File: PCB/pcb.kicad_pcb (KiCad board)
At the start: 2 copper layers, 3.9 x 3.7 mm, 320 parts, among them J1 USB_C_Receptacle_USB2.0, SW1 SW_Push, U1 AT90USB1286-AU, Y1 Crystal_GND24_Small

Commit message: Diode placement, Alternative Bottom Rows
-New Footprints
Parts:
- added MX101: MX-NoLED, kailh-switches-hotswap:Kailh-Hotswap-6.25U, F.Cu at (220.7, 361.9)
- added MX102: MX-NoLED, kailh-switches-hotswap:Kailh-Hotswap-7U, F.Cu at (227.8, 361.9)
- added MX103: MX-NoLED, kailh-switches-hotswap:Kailh-Hotswap-1U, F.Cu at (289.7, 361.9)
- added MX104: MX-NoLED, kailh-switches-hotswap:Kailh-Hotswap-1.25U, F.Cu at (306.4, 361.9)
- MX11: footprint kailh-switches-hotswap:Kailh-Hotswap-1.25U -> kailh-switches-hotswap:Kailh-Hotswap-1U
- MX6: footprint kailh-switches-hotswap:Kailh-Hotswap-1.25U -> kailh-switches-hotswap:Kailh-Hotswap-1.5U
- MX80: footprint kailh-switches-hotswap:Kailh-Hotswap-1U -> kailh-switches-hotswap:Kailh-Hotswap-2U
- MX88: footprint kailh-switches-hotswap:Kailh-Hotswap-2U -> kailh-switches-hotswap:Kailh-Hotswap-1U
- moved D95 570.5 mm to (455.6, 308.8), turned to 90 degrees
- moved D90 563.0 mm to (436.6, 308.8), turned to 90 degrees
- moved D85 555.2 mm to (417.5, 308.8), turned to 90 degrees
- moved D91 545.8 mm to (436.6, 327.8), turned to 90 degrees
- moved D86 544.5 mm to (417.5, 327.8), turned to 90 degrees
- moved D87 525.3 mm to (417.5, 346.9), turned to 90 degrees
- moved D88 515.9 mm to (427.0, 365.9), turned to 90 degrees
- moved D79 438.9 mm to (388.9, 265.9), turned to 90 degrees
- moved D1 431.6 mm to (93.7, 265.9), turned to 90 degrees
- moved D24 431.5 mm to (169.9, 289.7), turned to 90 degrees
- moved D39 431.2 mm to (236.5, 265.9), turned to 90 degrees
- moved D33 427.1 mm to (217.5, 265.9), turned to 90 degrees
- moved D50 414.9 mm to (265.1, 289.7), turned to 90 degrees
- moved D45 412.5 mm to (246.1, 289.7), turned to 90 degrees
- moved D7 411.7 mm to (112.7, 289.7), turned to 90 degrees
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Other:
- board size 3.9 x 3.7 mm -> 827.1 x 748.5 mm

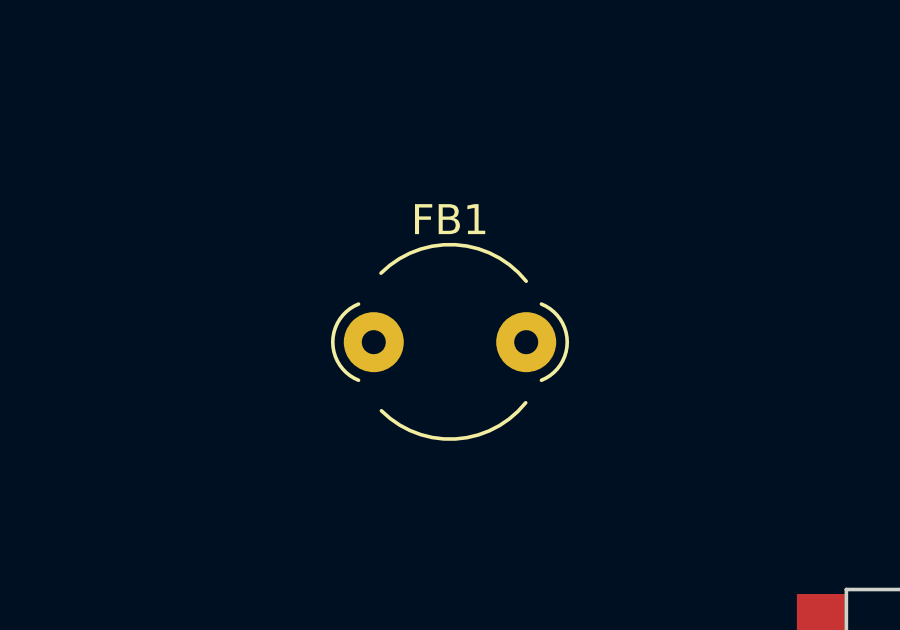
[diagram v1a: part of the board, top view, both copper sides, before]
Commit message: Changed Footprint for Ferrite
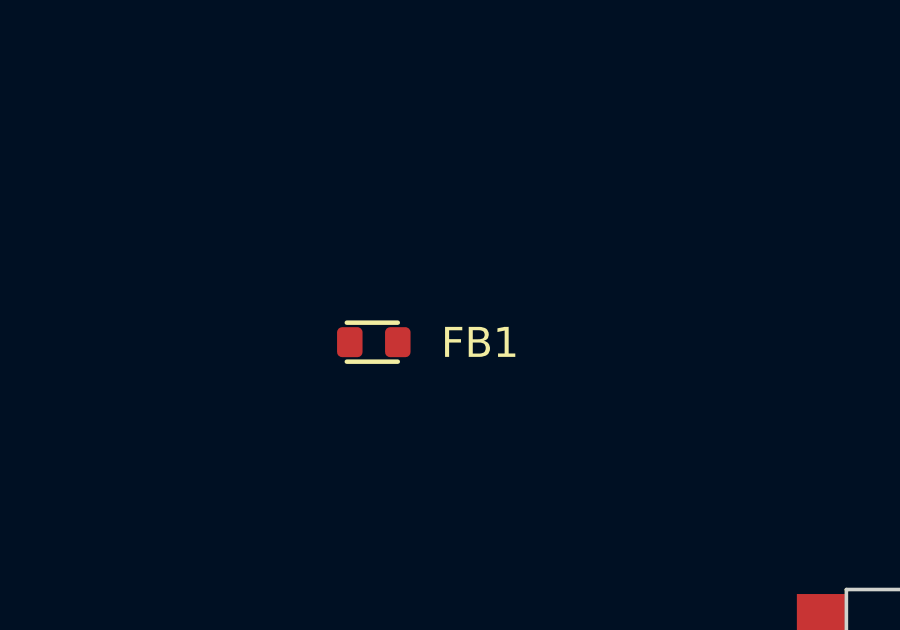
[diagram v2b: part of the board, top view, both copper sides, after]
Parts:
- FB1: footprint Ferrite_THT:LairdTech_28C0236-0JW-10 -> josh-passives-smt:Ferrite_Bead_0603
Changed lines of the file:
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@@
     )
   )
-  (footprint "Ferrite_THT:LairdTech_28C0236-0JW-10" (layer "F.Cu")
+  (footprint "josh-passives-smt:Ferrite_Bead_0603" (layer "F.Cu")
     (at 94.495332 474.8275)
-    (descr "Ferrite, vertical, LairdTech 28C0236-0JW-10, https://assets.lairdtech.com/home/brandworld/files/28C0236-0JW-10.pdf, JW Miller core https://www.bourns.com/products/magnetic-products/j.w.-miller-through-hole-ferrite-beads-emi-filters")
-    (tags "Ferrite vertical LairdTech 28C0236-0JW-10")
+    (descr "ferrite bead 0603")
+    (tags "Ferrite Bead")
     (property "Sheetfile" "pcb.kicad_sch")
     (property "Sheetname" "")
-    (attr through_hole)
-    (fp_text reference "FB1" (at 2.54 -4.064) (layer "F.SilkS")
+    (attr smd)
+    (fp_text reference "FB1" (at 3.542 0.028) (layer "F.SilkS")
       (effects (font (size 1 1) (thickness 0.15)))
     )
-    (fp_text value "600R" (at 2.54 4.953) (layer "F.Fab")
-      (effects (font (size 1 1) (thickness 0.15)))
+    (fp_text value "600R" (at 0 1.9) (layer "F.Fab") hide
+      (effects (font (size 1.27 1.27) (thickness 0.254)))
     )
-    (fp_text user "${REFERENCE}" (at 2.54 0) (layer "F.Fab")
-      (effects (font (size 1 1) (thickness 0.15)))
-    )
-    (fp_arc (start 5.588 -1.27) (mid 6.447832 0) (end 5.588 1.27) (layer "F.SilkS") (width 0.12))
-    (fp_arc (start 0.239932 -2.300068) (mid 2.71988 -3.24781) (end 5.08 -2.032) (layer "F.SilkS") (width 0.12))
-    (fp_arc (start 5.064465 2.019572) (mid 2.71878 3.227946) (end 0.254 2.286) (layer "F.SilkS") (width 0.12))
-    (fp_arc (start -0.508 1.27) (mid -1.367832 0) (end -0.508 -1.27) (layer "F.SilkS") (width 0.12))
-    (fp_circle (center 2.54 0) (end 6.48 0) (layer "F.CrtYd") (width 0.05) (fill none))
-    (fp_line (start 0 -1.145) (end 5.08 -1.145) (layer "F.Fab") (width 0.1))
-    (fp_line (start 0 1.145) (end 5.08 1.145) (layer "F.Fab") (width 0.1))
-    (fp_arc (start 0 1.145) (mid -1.145 0) (end 0 -1.145) (layer "F.Fab") (width 0.1))
-    (fp_arc (start 5.08 -1.145) (mid 6.225 0) (end 5.08 1.145) (layer "F.Fab") (width 0.1))
-    (fp_circle (center 2.54 0) (end 5.54 0) (layer "F.Fab") (width 0.1) (fill none))
-    (pad "1" thru_hole circle (at 0 0) (size 2 2) (drill 0.8) (layers *.Cu *.Mask)
+    (fp_line (start -0.9 -0.65) (end 0.8 -0.65) (layer "F.SilkS") (width 0.15))
+    (fp_line (start -0.9 0.65) (end 0.8 0.65) (layer "F.SilkS") (width 0.15))
+    (fp_line (start 0.8 -0.4) (end 0.8 0.4) (layer "Dwgs.User") (width 0.1))
+    (fp_line (start -0.8 0.4) (end -0.8 -0.4) (layer "Dwgs.User") (width 0.1))
+    (fp_line (start -1.475 0.75) (end -1.475 -0.75) (layer "F.CrtYd") (width 0.05))
+    (fp_line (start 1.475 0.75) (end -1.475 0.75) (layer "F.CrtYd") (width 0.05))
+    (fp_line (start -1.475 -0.75) (end 1.475 -0.75) (layer "F.CrtYd") (width 0.05))
+    (fp_line (start 1.475 -0.75) (end 1.475 0.75) (layer "F.CrtYd") (width 0.05))
+    (pad "1" smd roundrect (at -0.8 0) (size 0.85 1) (layers "F.Cu" "F.Paste" "F.Mask") (roundrect_rratio 0.2)
       (net 3 "+5V") (pintype "passive"))
-    (pad "2" thru_hole circle (at 5.08 0) (size 2 2) (drill 0.8) (layers *.Cu *.Mask)
+    (pad "2" smd roundrect (at 0.8 0) (size 0.85 1) (layers "F.Cu" "F.Paste" "F.Mask") (roundrect_rratio 0.2)
       (net 214 "Net-(F1-Pad1)") (pintype "passive"))
-    (model "${KICAD6_3DMODEL_DIR}/Ferrite_THT.3dshapes/LairdTech_28C0236-0JW-10.wrl"
+    (model "${KIPRJMOD}/../../josh-kicad-lib//packages3d/josh-passives-smt/BLM18PG121SZ1D.stp"
       (offset (xyz 0 0 0))
       (scale (xyz 1 1 1))

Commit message: Placed all LEDs
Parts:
- MX80: footprint kailh-switches-hotswap:Kailh-Hotswap-2U -> kailh-switches-hotswap:Kailh-Hotswap-1U
- MX88: footprint kailh-switches-hotswap:Kailh-Hotswap-1U -> kailh-switches-hotswap:Kailh-Hotswap-2U
- moved D196 624.6 mm to (462.8, 236.5)
- moved D199 590.3 mm to (481.8, 227.0)
- moved D154 563.8 mm to (310.4, 174.6)
- moved D189 554.7 mm to (443.7, 198.4)
- moved D139 543.5 mm to (243.7, 174.6)
- moved D168 540.8 mm to (338.9, 217.5)
- moved D192 528.7 mm to (443.7, 255.6)
- moved D185 513.3 mm to (424.7, 217.5)
- moved D169 510.0 mm to (343.7, 236.5)
- moved D194 508.0 mm to (462.8, 198.4)
- moved D118 494.0 mm to (158.0, 174.6)
- moved D155 481.2 mm to (291.3, 198.4)
- moved D184 470.3 mm to (424.7, 198.4)
- moved D182 465.8 mm to (396.1, 236.5)
- moved D144 463.3 mm to (262.7, 174.6)
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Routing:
- net +5V: track 26.6 -> 0.63 mm
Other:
- board size 827.1 x 748.5 mm -> 403.2 x 127 mm

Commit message: PCB Size, LED Footprints
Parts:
- D1, D10, D100, D11, D12, D13, D14, D15, D16, D17, D18, D19, D2, D20, D21, D22, D23, D24, D25, D26, D27, D28, D29, D3, D30, D31, D32, D33, D34, D35, D36, D37, D38, D39, D4, D40, D41, D42, D43, D44, D45, D46, D47, D48, D49, D5, D50, D51, D52, D53, D54, D55, D56, D57, D58, D59, D6, D60, D61, D62, D63, D64, D65, D66, D67, D68, D69, D7, D70, D71, D72, D73, D74, D75, D76, D77, D78, D79, D8, D80, D81, D82, D83, D84, D85, D86, D87, D88, D89, D9, D90, D91, D92, D93, D94, D95, D96, D97, D98, D99: footprint Diode_SMD:D_SOD-123 -> led:D_SOD-123
- D101, D102, D103, D104, D105, D106, D107, D108, D109, D110, D111, D112, D113, D114, D115, D116, D117, D118, D119, D120, D121, D122, D123, D124, D125, D126, D127, D128, D129, D130, D131, D132, D133, D134, D135, D136, D137, D138, D139, D140, D141, D142, D143, D144, D145, D146, D147, D148, D149, D150, D151, D152, D153, D154, D155, D156, D157, D158, D159, D160, D161, D162, D163, D164, D165, D166, D167, D168, D169, D170, D171, D172, D173, D174, D175, D176, D177, D178, D179, D180, D181, D182, D183, D184, D185, D186, D187, D188, D189, D190, D191, D192, D193, D194, D195, D196, D197, D198, D199, D200: footprint led:SK6812MINI_3.5x3.7mm_SMD -> led:SK6812MINI_3.5x3.7mm_SMD-Back
- J1: moved to B.Cu
- moved U1 212.8 mm to (453.2, 176.2), turned to 45 degrees
- moved J1 122.2 mm to (119.9, 165.9)
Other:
- outline, holes or cut-outs redrawn

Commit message: Copper Plates Backup (Simon)
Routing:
- net COL16: track 0.00 -> 55.8 mm
- net COL15: track 0.00 -> 46.5 mm
- net COL6: track 0.00 -> 31.2 mm
- net COL17: track 0.00 -> 27.9 mm
- net COL9: track 0.00 -> 21.8 mm
- net Net-(D59-Pad2): track 0.00 -> 20.1 mm
- net COL13: track 0.00 -> 18.6 mm
- net COL7: track 0.00 -> 18.6 mm
- net COL5: track 0.00 -> 18.6 mm
- net COL1: track 0.00 -> 18.6 mm
- net COL0: track 0.00 -> 18.6 mm
- net COL8: track 0.00 -> 18.6 mm
- net COL12: track 0.00 -> 18.6 mm
- net COL2: track 0.00 -> 18.6 mm
- net COL11: track 0.00 -> 18.6 mm
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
